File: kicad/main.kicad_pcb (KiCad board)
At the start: 2 copper layers, 162.2 x 137.3 mm, 44 parts, among them J1 Barrel_Jack, J2 UART, P1 Mini-DIN_6pins_ver3, SW1 Reset, U1 KM1810VM88, U10 L7805, U11 15 MHz, U12 8255, U13 uSD adapter, U14 8259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

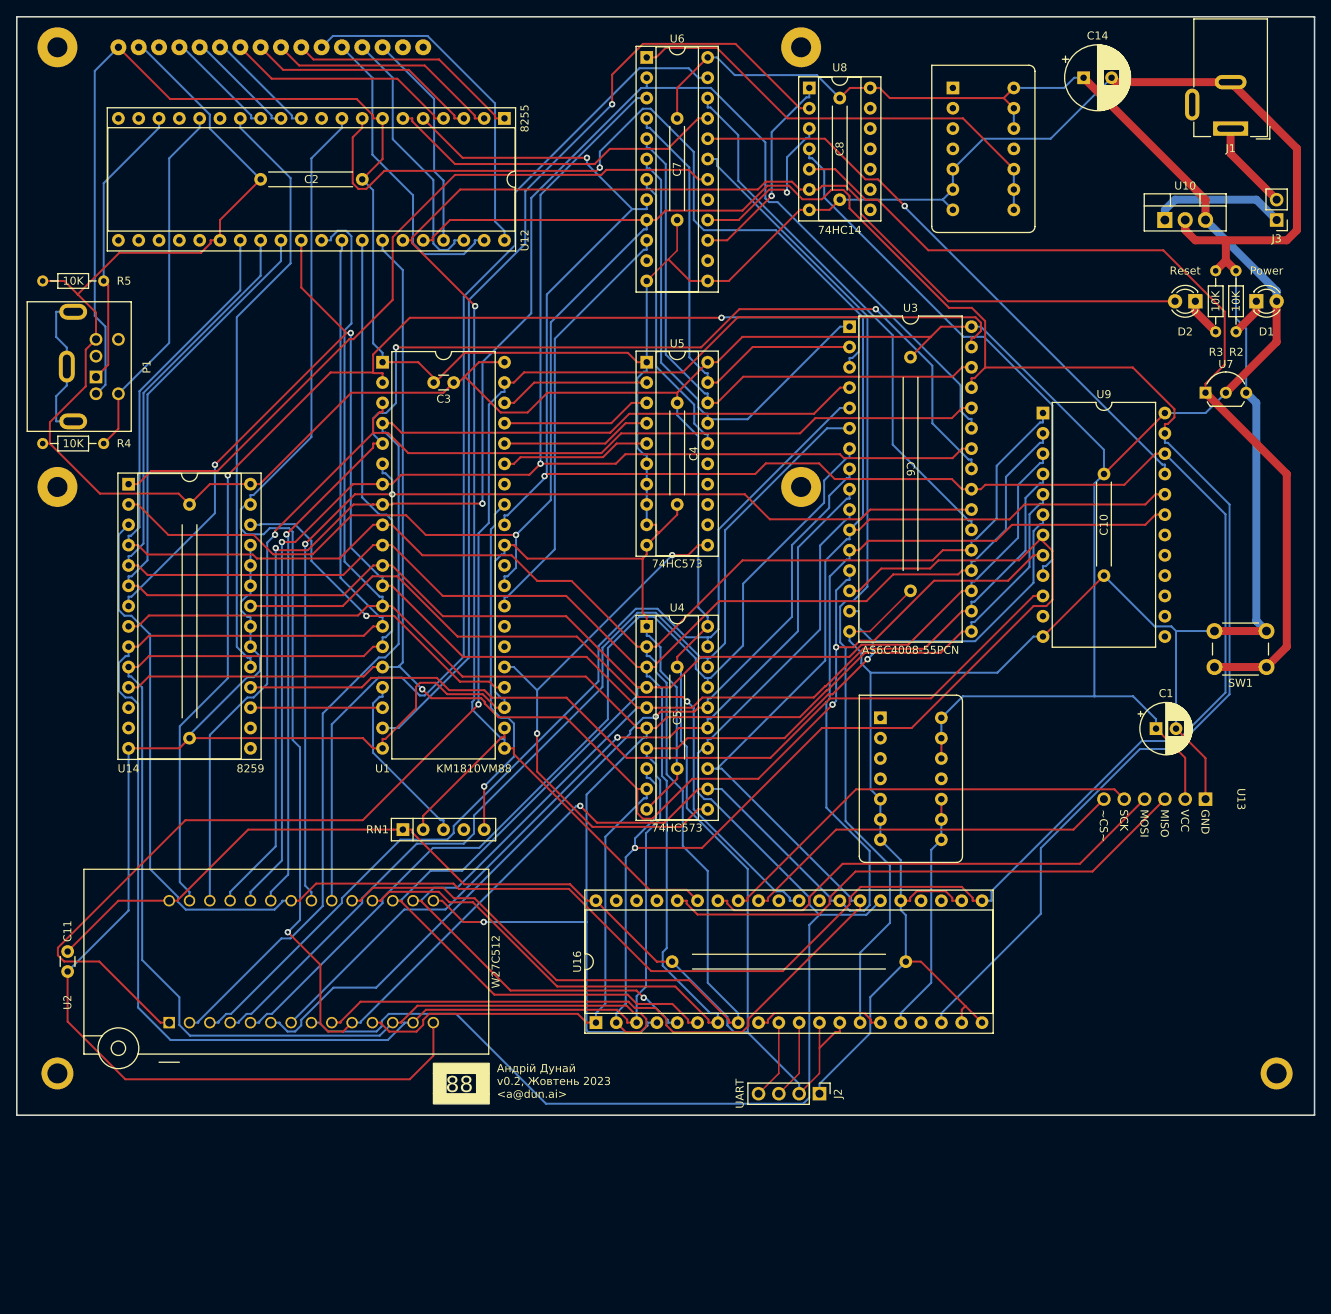
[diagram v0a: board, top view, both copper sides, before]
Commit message: 135x160 board
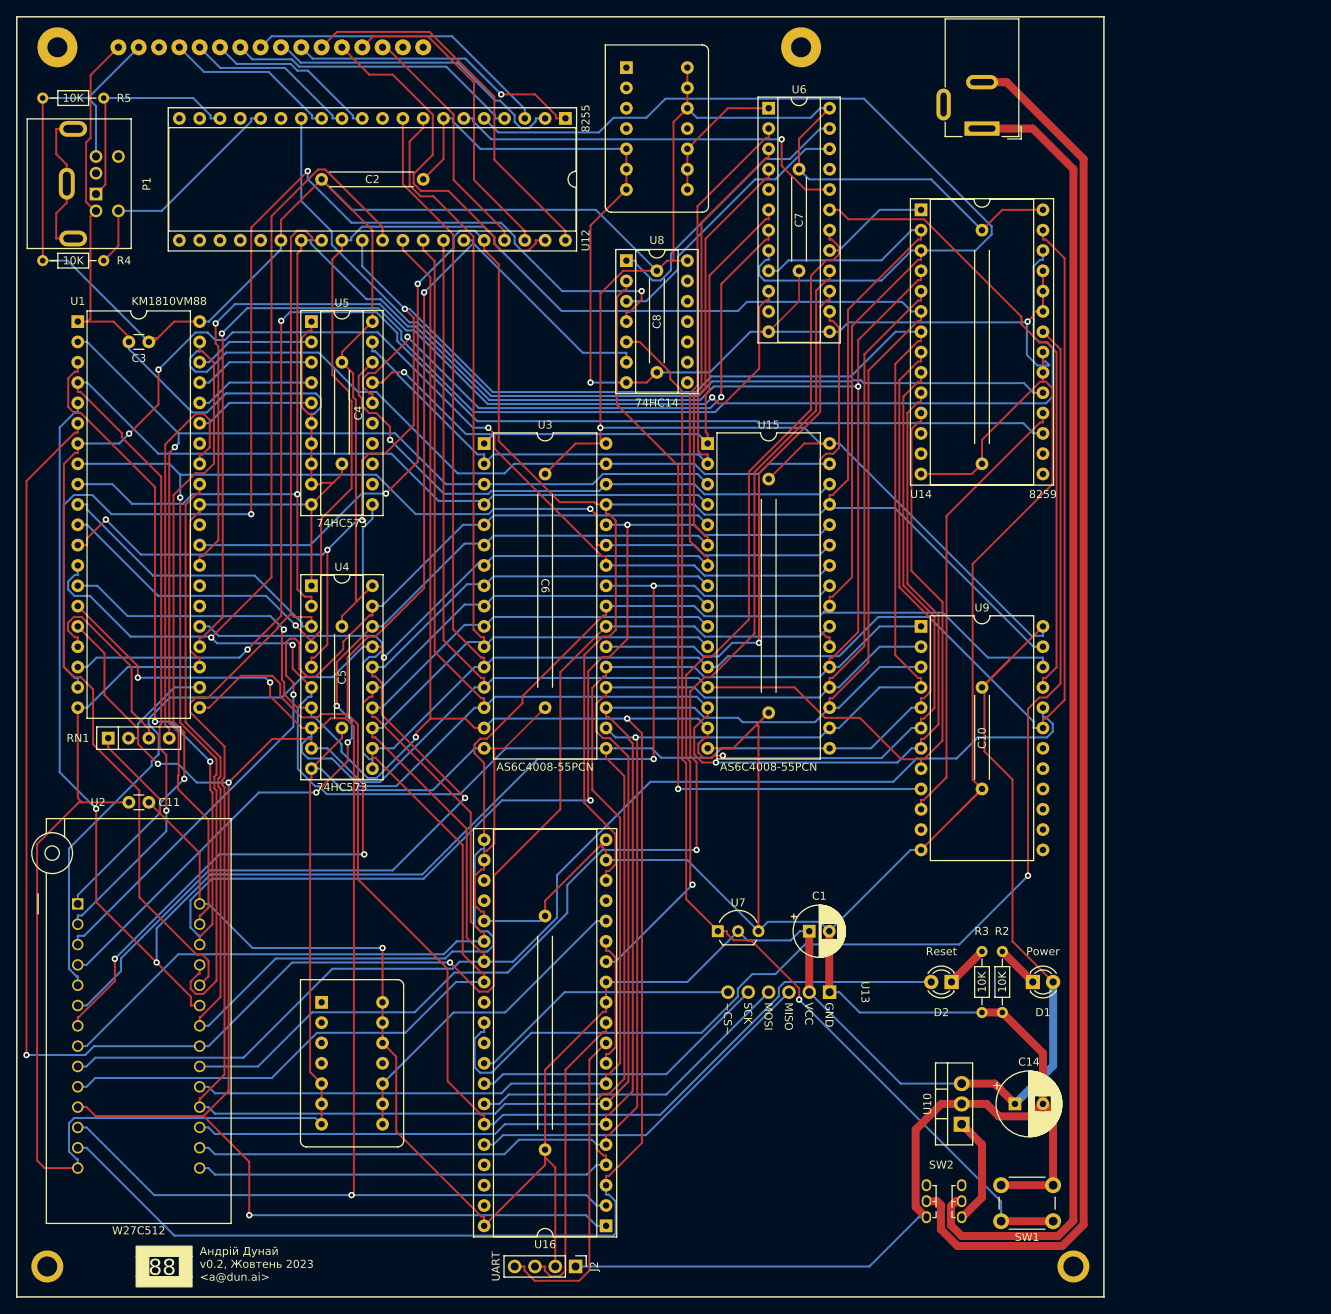
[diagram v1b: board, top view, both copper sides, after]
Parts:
- removed J3: ~, Connector_PinHeader_2.54mm:PinHeader_1x02_P2.54mm_Vertical
- added C13: 0.1 uF, footprints:C_Disc_VeryLong, F.Cu at (114.3, 81.9)
- added SW2: SW_Push_DPDT, footprints:PB22E06, F.Cu at (133.3, 163.0)
- added U15: AS6C4008-55PCN, Package_DIP:DIP-32_W15.24mm, F.Cu at (106.7, 71.1)
- RN1: value 5K -> R_Network03_Split; footprint Resistor_THT:R_Array_SIP5 -> Resistor_THT:R_Array_SIP4
- moved C14 128.6 mm to (145.1, 153.7)
- moved U10 115.8 mm to (138.4, 156.2), turned to 90 degrees
- moved C12 104.8 mm to (141.0, 50.8)
- moved U14 104.8 mm to (133.3, 41.9)
- moved U7 90.8 mm to (108.0, 132.1)
- moved D2 90.4 mm to (137.2, 138.4)
- moved D1 89.6 mm to (147.3, 138.4)
- moved R2 82.8 mm to (143.5, 134.6), turned to -90 degrees
- moved R3 82.8 mm to (141.0, 134.6), turned to -90 degrees
- moved U18 78.4 mm to (62.1, 148.6)
- moved SW1 74.2 mm to (149.9, 168.3)
- moved U13 52.8 mm to (127.6, 137.2)
- moved C1 50.2 mm to (119.4, 132.1)
- moved U3 48.0 mm to (78.7, 71.1)
- moved C6 48.0 mm to (86.4, 81.3)
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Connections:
- J1 pad 2: GND -> Net-(J1-Pad2)
- RN1 pad 4: unconnected-(RN1C-R3.2-Pad4) -> Net-(RN1C-R3.2)
- U1 pad 33: Net-(RN1D-R4.2) -> Net-(RN1C-R3.2)
- U12 pad 6: IO~{EN} -> PPI~{EN}
- U3 pad 22: RAM~{EN} -> LORAM~{EN}
- U6 pad 14: unconnected-(U6-I/O/Q-Pad14) -> HIRAM~{EN}
- U6 pad 15: Net-(U6-I/O/Q-Pad15) -> LORAM~{EN}
- U6 pad 16: Net-(U6-I/O/Q-Pad16) -> ROM~{EN}
- U6 pad 17: unconnected-(U6-I/O/Q-Pad17) -> INT~{EN}
- U6 pad 18: INT~{EN} -> UART~{EN}
- U6 pad 19: UART~{EN} -> TIMER~{EN}
- U6 pad 2: A_{8} -> A_{5}
- U6 pad 20: TIMER~{EN} -> PPI~{EN}
- U6 pad 21: IO~{EN} -> unconnected-(U6-I/O/Q-Pad21)
- U6 pad 22: RAM~{EN} -> Net-(U6-I/O/Q-Pad22)
- U6 pad 23: ROM~{EN} -> Net-(U6-I/O/Q-Pad23)
- U6 pad 3: A_{9} -> A_{6}
- U8 pad 1: Net-(U6-I/O/Q-Pad15) -> Net-(U6-I/O/Q-Pad23)
- U8 pad 2: CLK -> TIMERCLK
- U8 pad 3: Net-(U6-I/O/Q-Pad16) -> Net-(U6-I/O/Q-Pad22)
- U8 pad 4: TIMERCLK -> CLK
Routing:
- net Net-(J1-Pad2): track 0.00 -> 174.7 mm
- net Net-(J1-Pad1): track 11.3 -> 165.6 mm
- net INTR: track 16.5 -> 167.5 mm, vias 0 -> 2
- net ~{INTA}: track 41.7 -> 173.1 mm
- net AD_{3}: track 263.5 -> 368.8 mm, vias 1 -> 2
- net AD_{5}: track 279.4 -> 373.3 mm, vias 0 -> 1
- net A_{10}: track 137.1 -> 226.6 mm
- net AD_{0}: track 271.2 -> 357.9 mm
- net AD_{4}: track 278.6 -> 365.0 mm, vias 3 -> 5
- net AD_{6}: track 287.9 -> 368.2 mm
- net INT~{EN}: track 93.7 -> 13.5 mm
- net AD_{2}: track 306.4 -> 382.7 mm, vias 1 -> 4
- net GND: track 810.4 -> 881.9 mm, vias 0 -> 2
- net LORAM~{EN}: track 0.00 -> 68.2 mm, vias 0 -> 1
- net RAM~{EN}: track 68.1 -> 0.00 mm
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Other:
- board size 162.2 x 137.3 mm -> 135.9 x 160 mm

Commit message: PCB 2.0 RC
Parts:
- removed LCD1: ~, footprints:2004A-OLED
- added RV1: R_Potentiometer, Potentiometer_THT:Potentiometer_Bourns_3296Y_Vertical, F.Cu at (207.0, 67.3)
- added U17: T6963C, footprints:LCD24064, F.Cu at (21.8, 17.1)
- added U19: ATF16V8, Package_DIP:DIP-20_W7.62mm_Socket, F.Cu at (73.7, 53.3)
- C1: value 10 uF -> 0.1 uF; footprint Capacitor_THT:CP_Radial_D6.3mm_P2.50mm -> footprints:C_Disc_Long
- U12: footprint Package_DIP:DIP-40_W15.24mm_Socket -> Package_DIP:DIP-40_W15.24mm
- U6: value GAL22V10 -> ATF16V8; footprint Package_DIP:DIP-24_W7.62mm_Socket -> Package_DIP:DIP-20_W7.62mm_Socket
- moved P1 185.6 mm to (215.6, 47.9)
- moved R4 185.6 mm to (209.0, 56.2)
- moved R5 185.6 mm to (209.0, 35.9)
- moved U16 151.4 mm to (142.2, 25.4), turned to 0 degrees
- moved C9 128.5 mm to (149.9, 41.3), turned to -90 degrees
- moved SW2 128.1 mm to (212.1, 61.9)
- moved C2 119.4 mm to (176.5, 55.9), turned to 90 degrees
- moved U10 113.2 mm to (215.9, 73.7), turned to 180 degrees
- moved U18 108.3 mm to (149.9, 85.3), turned to 0 degrees
- moved C14 96.2 mm to (209.9, 82.5)
- moved U7 89.5 mm to (193.0, 104.4), turned to 90 degrees
- moved H2 88.1 mm to (217.2, 114.3)
- moved J2 88.0 mm to (152.4, 111.8)
- moved SW1 86.2 mm to (207.0, 103.8)
- moved U11 84.8 mm to (149.9, 100.5), turned to 0 degrees
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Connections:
- U12 pad 1: Net-(LCD1-D_{3}) -> unconnected-(U12-PA3-Pad1)
- U12 pad 11: Net-(LCD1-E) -> unconnected-(U12-PC6-Pad11)
- U12 pad 12: Net-(LCD1-R~{W}) -> unconnected-(U12-PC5-Pad12)
- U12 pad 13: Net-(LCD1-RS) -> unconnected-(U12-PC4-Pad13)
- U12 pad 2: Net-(LCD1-D_{2}) -> unconnected-(U12-PA2-Pad2)
- U12 pad 3: Net-(LCD1-D_{1}) -> unconnected-(U12-PA1-Pad3)
- U12 pad 37: Net-(LCD1-D_{7}) -> unconnected-(U12-PA7-Pad37)
- U12 pad 38: Net-(LCD1-D_{6}) -> unconnected-(U12-PA6-Pad38)
- U12 pad 39: Net-(LCD1-D_{5}) -> unconnected-(U12-PA5-Pad39)
- U12 pad 4: Net-(LCD1-D_{0}) -> unconnected-(U12-PA0-Pad4)
- U12 pad 40: Net-(LCD1-D_{4}) -> unconnected-(U12-PA4-Pad40)
- U14 pad 1: INT~{EN} -> PIC~{EN}
- U6 pad 10: IO/~{M} -> GND
- U6 pad 11: unconnected-(U6-I-Pad11) -> GND
- U6 pad 12: GND -> unconnected-(U6-I/O-Pad12)
- U6 pad 13: GND -> unconnected-(U6-I/O-Pad13)
- U6 pad 17: INT~{EN} -> unconnected-(U6-I/O-Pad17)
- U6 pad 18: UART~{EN} -> Net-(U6-I/O-Pad18)
- U6 pad 19: TIMER~{EN} -> Net-(U6-I/O-Pad19)
- U6 pad 2: A_{5} -> A_{16}
- U6 pad 20: PPI~{EN} -> +5V
- U6 pad 3: A_{6} -> A_{17}
- U6 pad 4: A_{16} -> A_{18}
- U6 pad 5: A_{17} -> A_{19}
- U6 pad 6: A_{18} -> IO/~{M}
- U6 pad 7: A_{19} -> unconnected-(U6-I-Pad7)
- U6 pad 8: ~{RD} -> unconnected-(U6-I-Pad8)
- U6 pad 9: ~{WR} -> unconnected-(U6-I-Pad9)
- U8 pad 1: Net-(U6-I/O/Q-Pad23) -> Net-(U6-I/O-Pad19)
- U8 pad 3: Net-(U6-I/O/Q-Pad22) -> Net-(U6-I/O-Pad18)
- U9 pad 21: TIMER~{EN} -> PIT~{EN}
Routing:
- net LCD~{EN}: track 0.00 -> 170.4 mm, vias 0 -> 1
- net MCLK: track 17.3 -> 167.1 mm, vias 0 -> 1
- net Net-(J1-Pad2): track 174.7 -> 44.1 mm
- net Net-(U6-I/O-Pad18): track 0.00 -> 108.0 mm, vias 0 -> 1
- net ~{INTA}: track 173.1 -> 67.3 mm
- net GND: track 881.9 -> 777.3 mm, vias 2 -> 0
- net Net-(U6-I/O-Pad19): track 0.00 -> 99.0 mm, vias 0 -> 1
- net Net-(J1-Pad1): track 165.6 -> 68.7 mm
- net INT4: track 157.7 -> 69.8 mm, vias 1 -> 2
- net A_{1}: track 301.1 -> 218.1 mm, vias 0 -> 2
- net TIMER~{EN}: track 79.1 -> 0.00 mm
- net ROM~{EN}: track 156.0 -> 84.2 mm
- net CLK: track 148.4 -> 77.0 mm, vias 3 -> 1
- net A_{19}: track 78.8 -> 10.2 mm, vias 2 -> 0
- net A_{0}: track 327.4 -> 261.9 mm, vias 0 -> 1
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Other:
- board size 135.9 x 160 mm -> 200 x 100 mm

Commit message: Cleaner PCB
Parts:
- H1, H2: footprint footprints:Hole_2.5x4 -> footprints:Hole_3.5x5
- moved RN1 3.59 mm to (34.9, 80.0)
- moved C1 2.54 mm to (80.0, 58.4)
- moved C7 2.54 mm to (80.0, 27.9)
- moved U19 2.54 mm to (76.2, 53.3)
- moved U3 2.54 mm to (94.0, 25.4)
- moved U6 2.54 mm to (76.2, 22.9)
- moved U1 2.54 mm to (31.1, 25.4)
- moved C3 2.54 mm to (40.0, 27.9)
- moved C4 2.54 mm to (62.2, 27.9)
- moved C5 2.54 mm to (62.2, 58.4)
- moved U4 2.54 mm to (58.4, 53.3)
- moved U5 2.54 mm to (58.4, 22.9)
- moved C14 2.54 mm to (212.4, 82.5)
- moved C6 2.54 mm to (101.6, 35.6)
- moved D1 1.27 mm to (205.7, 90.2)
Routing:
- net Net-(U6-I/O-Pad19): track 99.0 -> 200.0 mm, vias 1 -> 0
- net AD_{0}: track 382.7 -> 329.7 mm, vias 3 -> 2
- net PIT~{EN}: track 57.1 -> 90.9 mm, vias 1 -> 0
- net AD_{1}: track 347.3 -> 315.1 mm
- net LCD~{EN}: track 170.4 -> 140.3 mm, vias 1 -> 0
- net ~{WR}: track 293.0 -> 322.7 mm
- net A_{0}: track 261.9 -> 289.2 mm, vias 1 -> 4
- net A_{2}: track 172.8 -> 199.4 mm, vias 3 -> 1
- net AD_{3}: track 304.1 -> 330.3 mm
- net Net-(J1-Pad1): track 68.7 -> 43.6 mm
- net A_{8}: track 181.7 -> 158.3 mm, vias 2 -> 3
- net AD_{4}: track 319.2 -> 340.1 mm, vias 1 -> 3
- net A_{1}: track 218.1 -> 238.1 mm, vias 2 -> 3
- net Net-(U6-I/O-Pad18): track 108.0 -> 88.8 mm, vias 1 -> 3
- net A_{11}: track 172.9 -> 190.5 mm, vias 1 -> 3
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
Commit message: Even better PCB
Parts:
- moved U9 29.0 mm to (94.0, 86.4), turned to 0 degrees
- moved C8 25.9 mm to (95.2, 74.9), turned to 0 degrees
- moved U14 22.7 mm to (116.8, 81.3), turned to 0 degrees
- moved U8 21.7 mm to (94.0, 78.7), turned to 90 degrees
- moved C12 20.1 mm to (124.5, 90.2), turned to -90 degrees
- moved RN1 14.9 mm to (25.4, 68.6), turned to 90 degrees
- moved C10 14.8 mm to (101.6, 94.0), turned to -90 degrees
- moved C11 5.68 mm to (30.5, 100.3)
- moved U2 5.68 mm to (43.2, 109.2)
- moved J2 2.84 mm to (153.7, 114.3)
- moved U11 2.54 mm to (149.9, 103.0)
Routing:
- net Net-(U6-I/O-Pad19): track 200.0 -> 84.5 mm, vias 0 -> 1
- net ~{WR}: track 322.7 -> 255.3 mm, vias 2 -> 4
- net AD_{4}: track 340.1 -> 282.7 mm, vias 3 -> 0
- net RES: track 292.2 -> 241.2 mm
- net INTR: track 104.2 -> 141.1 mm, vias 1 -> 0
- net A_{0}: track 289.2 -> 255.7 mm, vias 4 -> 1
- net AD_{3}: track 330.3 -> 297.0 mm
- net ~{INTA}: track 61.5 -> 94.6 mm, vias 1 -> 0
- net ~{RD}: track 334.0 -> 301.0 mm, vias 2 -> 4
- net A_{1}: track 238.1 -> 206.7 mm
- net Net-(U16-RCLK): track 18.9 -> 47.5 mm, vias 1 -> 0
- net A_{2}: track 199.4 -> 171.6 mm
- net PIT~{EN}: track 90.9 -> 64.5 mm, vias 0 -> 1
- net AD_{2}: track 321.0 -> 295.8 mm
- net LORAM~{EN}: track 32.4 -> 56.9 mm, vias 2 -> 1
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
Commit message: Update logo
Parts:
- added kibuzzard-65254FD7: G***, kibuzzard-65254FD7, F.Cu at (195.6, 110.5)
- added kibuzzard-65254FDB: G***, kibuzzard-65254FDB, F.Cu at (205.7, 110.5)
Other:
- board text added: "Андрій Дунай <a@dun.ai> v0.2, Жовтень 2023"
- board text removed: "88"
- board text removed: "Андрій Дунай v0.2, Жовтень 2023 <a@dun.ai>"

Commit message: Final PCB
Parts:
- U15: value AS6C4008-55PCN -> RAM2 (AS6C4008)
- U2: value W27C512 -> ROM (W27C512)
- U3: value AS6C4008-55PCN -> RAM1 (AS6C4008)
- moved J2 7.73 mm to (146.1, 113.0), turned to 90 degrees
- moved C3 6.99 mm to (40.0, 21.0)
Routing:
- net Net-(J2-Pin_4): track 69.2 -> 79.9 mm
- net +5V: track 688.2 -> 696.8 mm
